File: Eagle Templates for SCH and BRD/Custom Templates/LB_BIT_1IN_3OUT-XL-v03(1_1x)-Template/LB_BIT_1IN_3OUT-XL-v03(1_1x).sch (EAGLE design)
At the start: 24 parts, among them U1 LV321SOT23-5, U2 LV321SOT23-5, U3 LV321SOT23-5

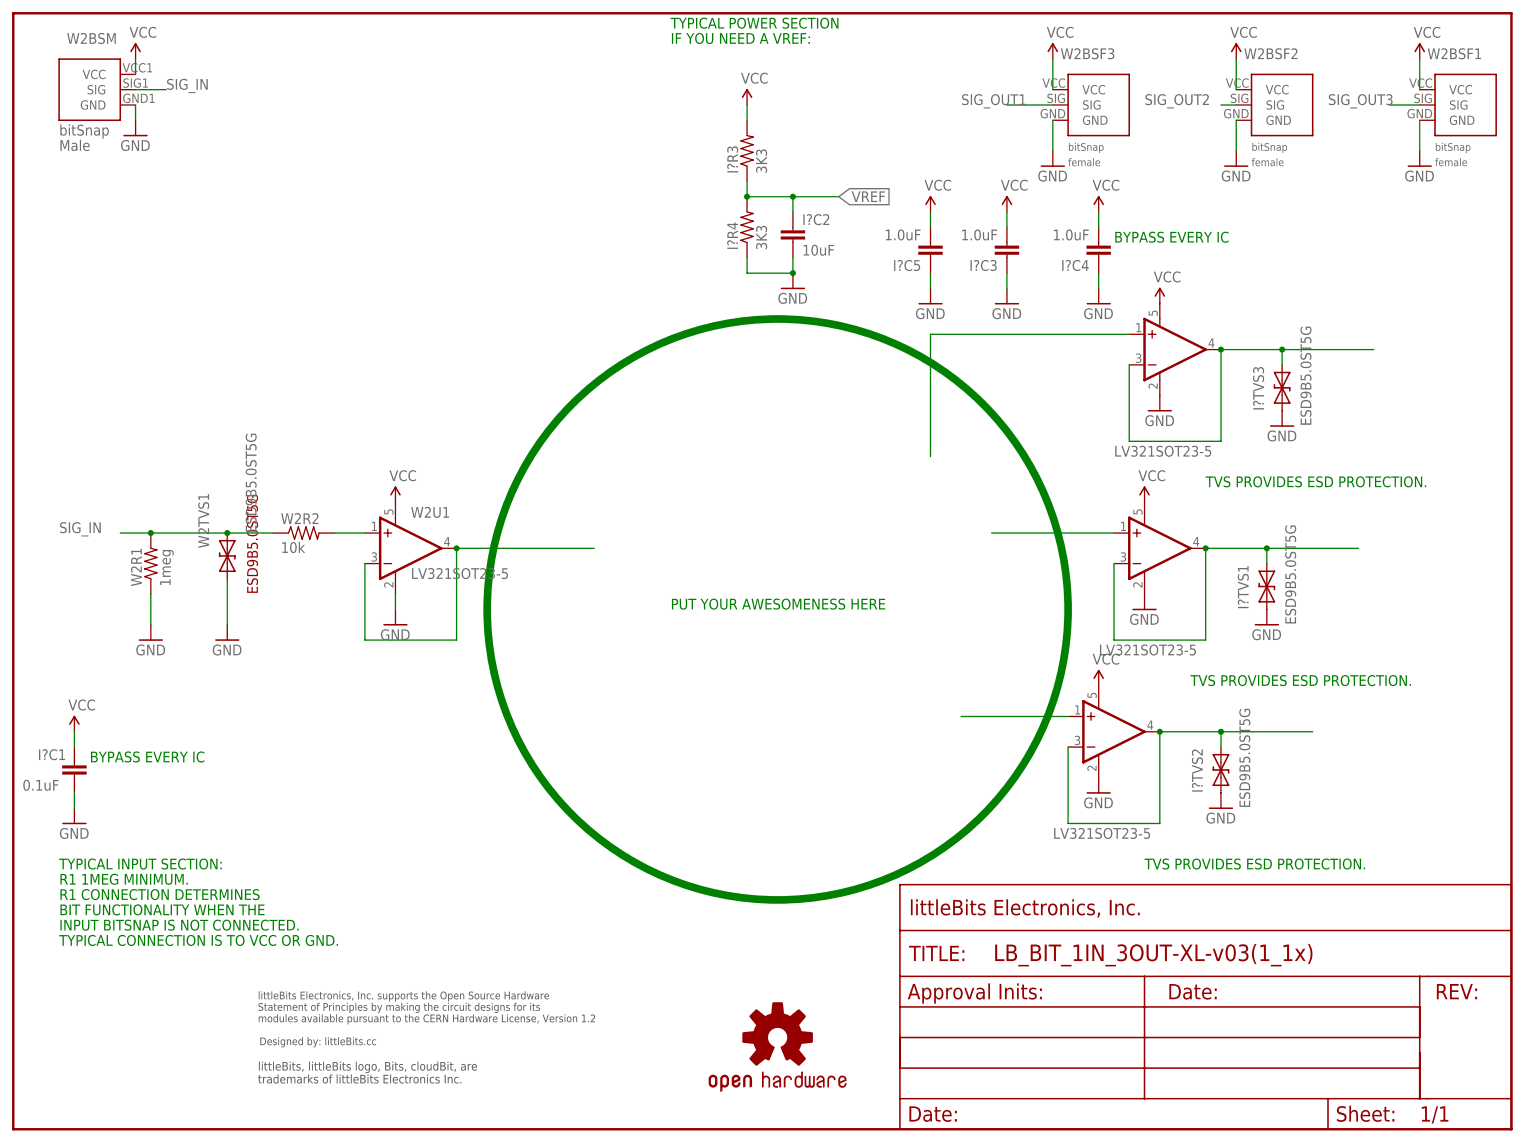
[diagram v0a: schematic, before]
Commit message: Updated templates
- Added ferrite beads
- Moved text and annotations off of Nets layer
- Minor layout changes
- Removed I/O/W prefix from reference designators
- Removed output stage components from output bits
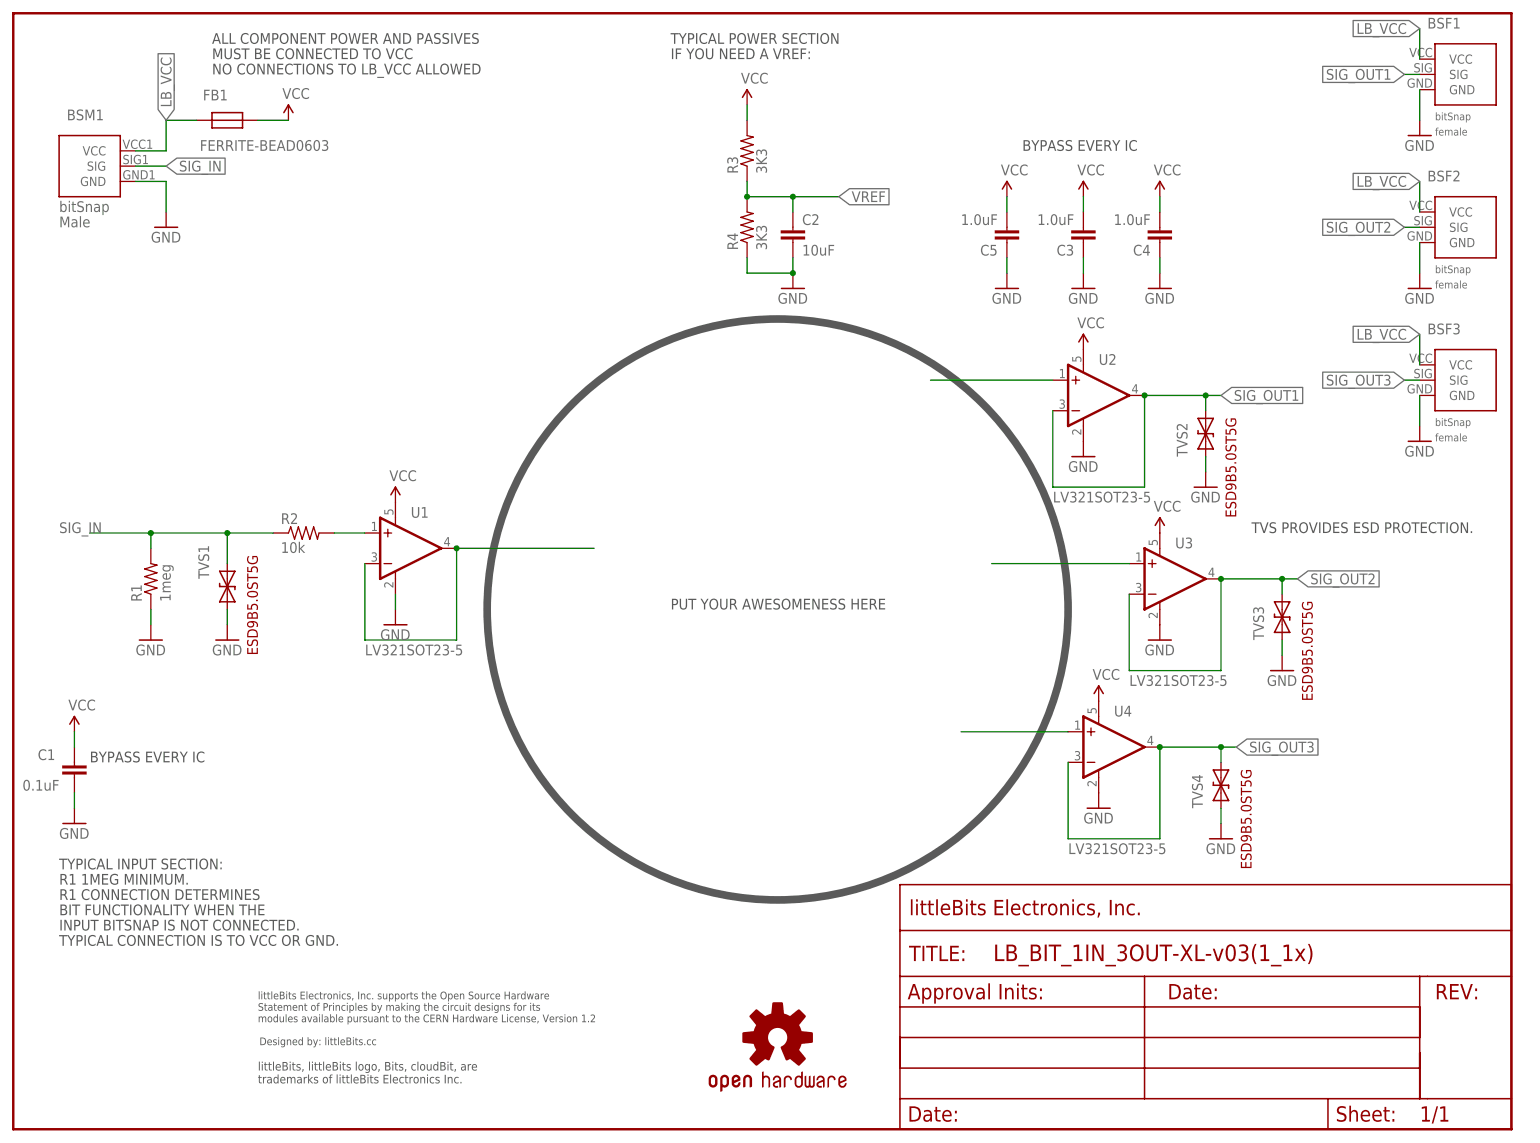
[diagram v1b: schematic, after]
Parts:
- removed I?C3, I?C4, I?C5: 1.0uF, LITTLEBITS:CAPCAP-0603
- removed I?TVS1, I?TVS2, I?TVS3, W2TVS1: ESD9B5.0ST5G, LITTLEBITS:DIODE-TVSSOD-923
- removed W2BSF1, W2BSF2, W2BSF3: BITSNAP_V03_FEMALE, bitSnap:BITSNAP_V03_FEMALE
- removed W2BSM: BITSNAP_V03_MALE, bitSnap:BITSNAP_V03_MALE
- removed W2R1: 1meg, LITTLEBITS:RESISTOR0603
- removed W2U1: LV321SOT23-5, LITTLEBITS:LV321SOT23-5
- added BSF1, BSF2, BSF3: BITSNAP_V03_FEMALE, bitSnap:BITSNAP_V03_FEMALE
- added BSM1: BITSNAP_V03_MALE, bitSnap:BITSNAP_V03_MALE
- added C3, C4, C5: 1.0uF, LITTLEBITS:CAPCAP-0603
- added FB1: FERRITE-BEAD0603, LITTLEBITS:FERRITE-BEAD0603
- added R1: 1meg, LITTLEBITS:RESISTOR0603
- added TVS1, TVS2, TVS3, TVS4: (no value), LITTLEBITS:DIODE-TVSSOD-923
- added U4: LV321SOT23-5, LITTLEBITS:LV321SOT23-5
- renumbered I?C1 to C1, I?C2 to C2, I?R3 to R3, I?R4 to R4, W2R2 to R2
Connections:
- removed net N$1 (its old number): U1.+IN
- new net LB_VCC: BSF1.VCC, BSF2.VCC, BSF3.VCC, BSM1.VCC, FB1.P$2
- new net N$5: U4.+IN
- net GND: now also BSF1.GND, BSF2.GND, BSF3.GND, BSM1.GND, C3.1, C4.1, C5.1, R1.1, TVS1.A, TVS2.A, TVS3.A, TVS4.A, U4.V-; no longer I?C3.1, I?C4.1, I?C5.1, I?TVS1.A, I?TVS2.A, I?TVS3.A, W2BSF1.GND, W2BSF2.GND, W2BSF3.GND, W2BSM.GND, W2R1.1, W2TVS1.A, W2U1.V-
- net N$2: now also U1.-IN, U1.OUT; no longer W2U1.-IN, W2U1.OUT
- net N$3: now also U1.+IN; no longer W2U1.+IN
- net SIG_IN: now also BSM1.SIG, R1.2, TVS1.C; no longer W2BSM.SIG, W2R1.2, W2TVS1.C
- net SIG_OUT1: now also BSF1.SIG, TVS2.C, U2.-IN, U2.OUT; no longer I?TVS3.C, U3.-IN, U3.OUT, W2BSF3.SIG
- net SIG_OUT2: now also BSF2.SIG, TVS3.C, U3.-IN, U3.OUT; no longer I?TVS1.C, U1.-IN, U1.OUT, W2BSF2.SIG
- net SIG_OUT3: now also BSF3.SIG, TVS4.C, U4.-IN, U4.OUT; no longer I?TVS2.C, U2.-IN, U2.OUT, W2BSF1.SIG
- net VCC: now also C3.2, C4.2, C5.2, FB1.P$1, U4.V+; no longer I?C3.2, I?C4.2, I?C5.2, W2BSF1.VCC, W2BSF2.VCC, W2BSF3.VCC, W2BSM.VCC, W2U1.V+
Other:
- note added: "ALL COMPONENT POWER AND PASSIVES"
- note added: "MUST BE CONNECTED TO VCC"
- note added: "NO CONNECTIONS TO LB_VCC ALLOWED"
